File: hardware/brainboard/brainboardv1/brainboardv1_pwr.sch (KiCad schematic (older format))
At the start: 31 parts, among them P11 JST, P12 CONN_4, P13 VBAT, P14 ~ALRT, P6 -3V3, P8 +2V5, P9 -2V5, U10 TPS60403, U11 TPS73225, U12 TPS72325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

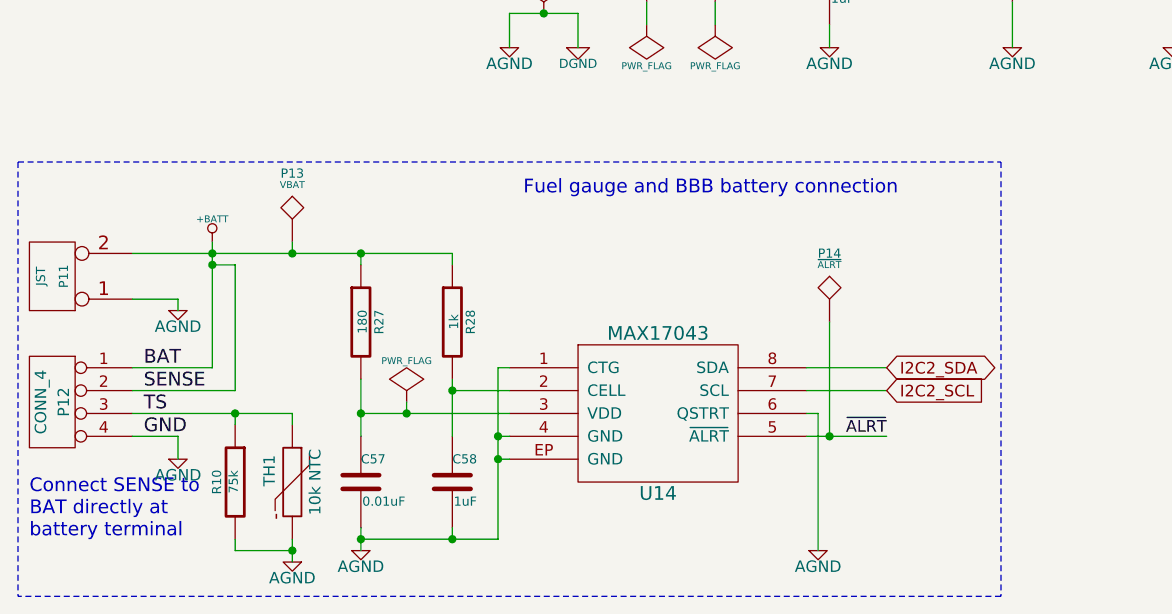
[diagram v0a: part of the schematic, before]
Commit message: Thesis version
Finally able to commit again (Windows XP issues fixed by OS upgrade).
Added latest version of wearable BB, along with prototype "muscleboard"
2-channel board for EMG/ECG applications
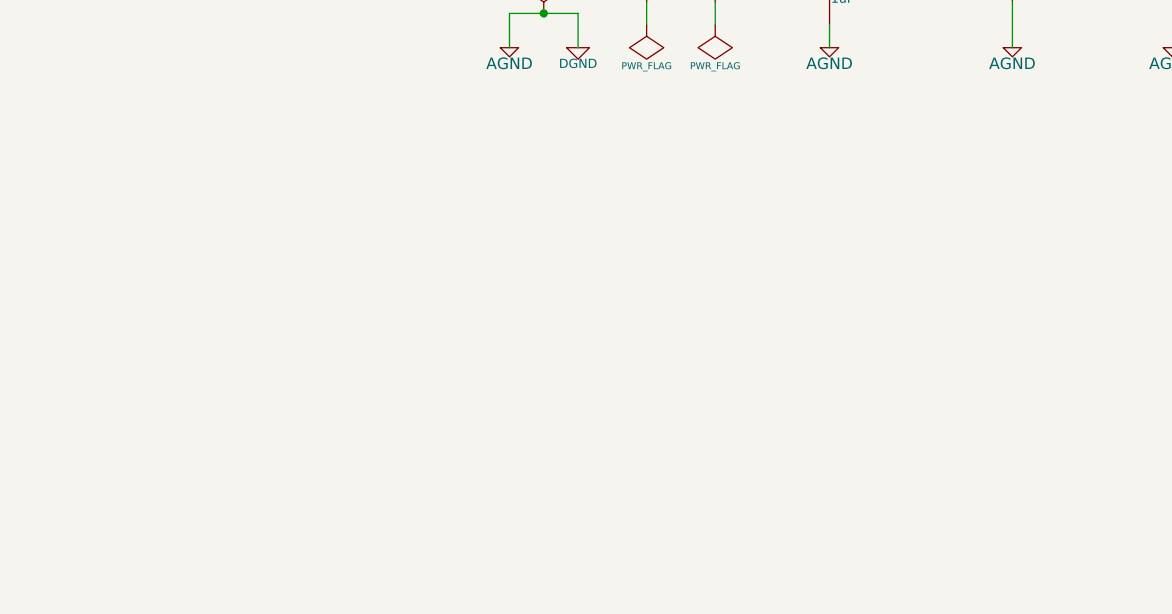
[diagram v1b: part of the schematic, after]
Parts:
- removed C57: 0.01uF, ~, symbol C
- removed C58: 1uF, ~, symbol C
- removed P11: JST, ~, symbol CONN_2
- removed P12: CONN_4, ~, symbol CONN_4
- removed P13: VBAT, ~, symbol TST
- removed P14: ~ALRT, ~, symbol TST
- removed R10: 75k, ~, symbol R
- removed R27: 180, ~, symbol R
- removed R28: 1k, ~, symbol R
- removed TH1: 10k NTC, ~, symbol THERMISTOR
- removed U14: MAX17043, ~, symbol MAX17043
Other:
- note removed: "Connect SENSE to\nBAT directly at\nbattery terminal"
- note removed: "Fuel gauge and BBB battery connection"
